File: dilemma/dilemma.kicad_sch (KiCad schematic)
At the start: 72 parts, among them J2 Serial, J4 Conn_01x01_Female, J5 S3B-PH-SM4-TB(LF)(SN), J7 trackball, SW1 SW_Push, SW10 SW_Push, SW11 SW_Push, SW12 SW_Push, SW13 SW_Push, SW14 SW_Push, SW15 SW_Push, SW16 SW_Push, SW17 SW_Push, SW2 SW_Push, SW26 SW_SPST, SW3 SW_Push, SW37 SW_SPST, SW4 SW_Push, SW5 SW_Push, SW6 SW_Push, SW7 SW_Push, SW8 SW_Push, SW9 SW_Push, U2 eliteC

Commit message: add battery connector
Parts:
- added H5, H6, H7, H8, H9: M4, footprints:MountingHole_3mm_Pad_thin, symbol Mechanical:MountingHole_Pad
- added J1: S3B-PH-SM4-TB(LF)(SN), Connector_JST:JST_PH_S3B-PH-SM4-TB_1x03-1MP_P2.00mm_Horizontal, symbol Connector:Conn_01x03_Female
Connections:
- net GND: now also H5.1, H6.1, H7.1, H8.1, H9.1
- net GND2: now also J1.1 (Pin_1), J1.3 (Pin_3)
- net bat_l: now also J1.2 (Pin_2)
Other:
- note added: "Mod screws"
- moved on the sheet: BT1, H1, H2, H3, H4, PSW1

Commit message: silkscreen
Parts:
- O2: footprint swoop:OLED_jumpers -> footprints:PinHeader_1x04_P2.54mm_Vertical
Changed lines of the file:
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@@
     (property "Reference" "O2" (id 0) (at 299.72 150.8275 0))
     (property "Value" "OLED" (id 1) (at 300.99 153.3675 0))
-    (property "Footprint" "swoop:OLED_jumpers" (id 2) (at 295.91 151.638 0)
+    (property "Footprint" "footprints:PinHeader_1x04_P2.54mm_Vertical" (id 2) (at 295.91 151.638 0)
       (effects (font (size 1.27 1.27)) hide)
     )
@@
     )
     (path "/c51d5d6e-3b88-4f8e-8052-c5e71c69581c"
-      (reference "O2") (unit 1) (value "OLED") (footprint "swoop:OLED_jumpers")
+      (reference "O2") (unit 1) (value "OLED") (footprint "footprints:PinHeader_1x04_P2.54mm_Vertical")
     )
     (path "/7b8c700f-e98a-4d4d-a6e4-baf976482a3f"

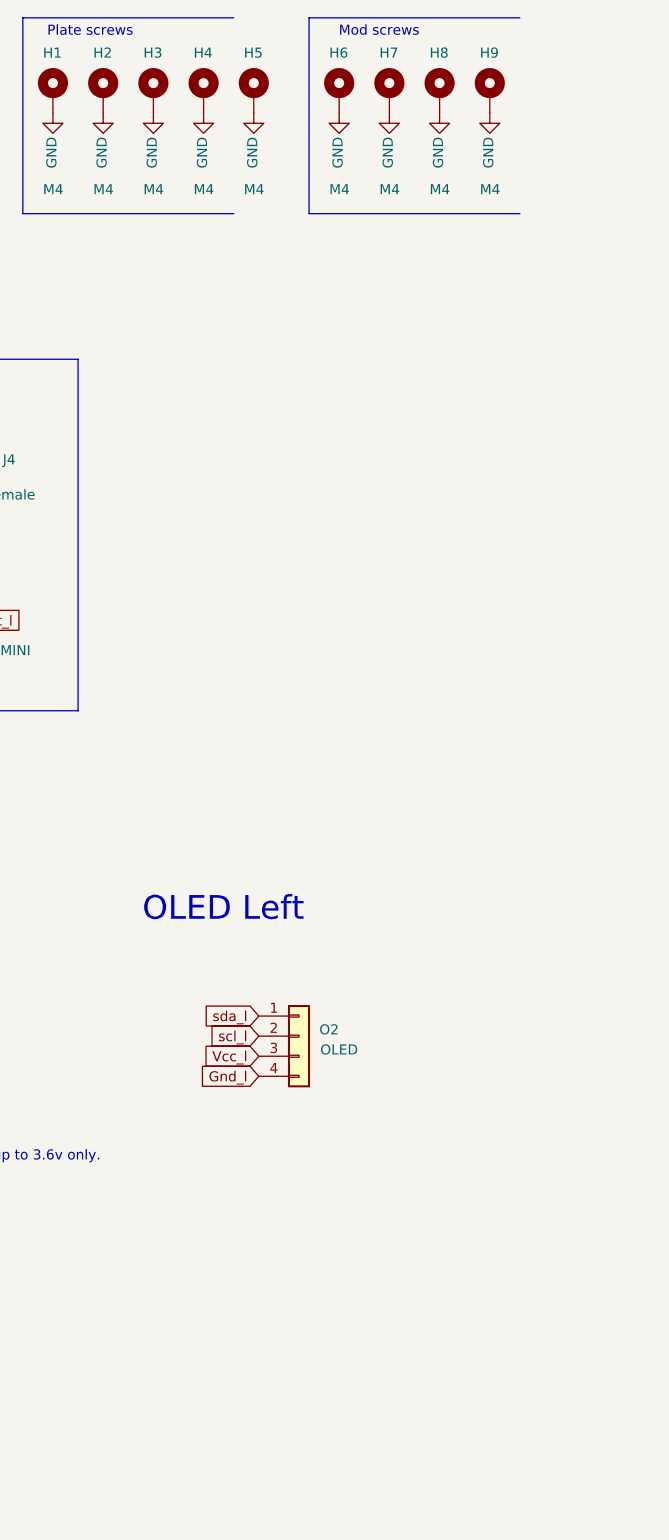
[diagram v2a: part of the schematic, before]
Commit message: trackpad connector reversible
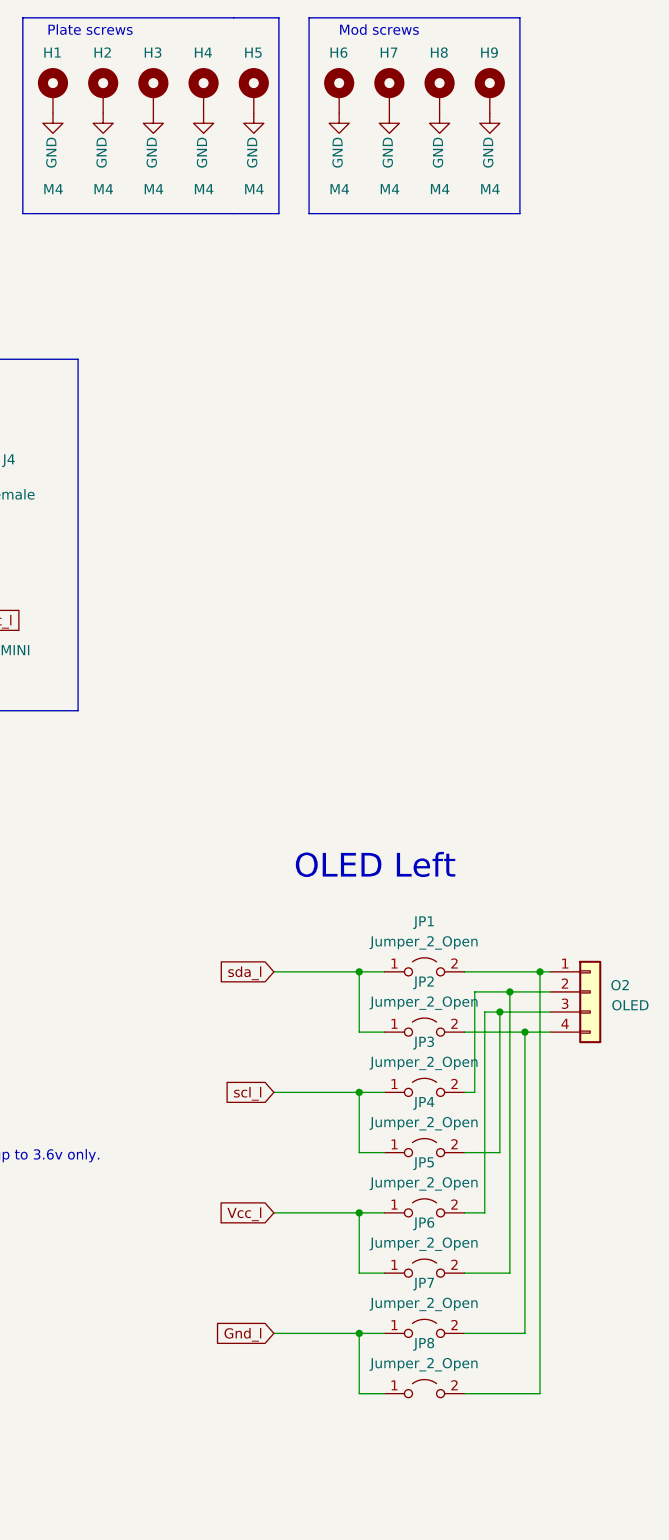
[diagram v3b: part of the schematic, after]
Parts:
- added JP1, JP2, JP3, JP4, JP5, JP6, JP7, JP8: Jumper_2_Open, footprints:SolderJumper-2_P1.3mm_Open_RoundedPad1.0x1.5mm, symbol Jumper:Jumper_2_Open
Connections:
- net +5VL: now also JP5.1 (A), JP6.1 (A); no longer O2.3 (Pin_3)
- net GND2: now also JP7.1 (A), JP8.1 (A); no longer O2.4 (Pin_4)
- net scl_l: now also JP3.1 (A), JP4.1 (A); no longer O2.2 (Pin_2)
- net sda_l: now also JP1.1 (A), JP2.1 (A); no longer O2.1 (Pin_1)
- new net: JP3.2 (B), JP6.2 (B), O2.2 (Pin_2)
- new net: JP4.2 (B), JP5.2 (B), O2.3 (Pin_3)
- new net: JP2.2 (B), JP7.2 (B), O2.4 (Pin_4)
- new net: JP1.2 (B), JP8.2 (B), O2.1 (Pin_1)
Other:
- moved on the sheet: O2

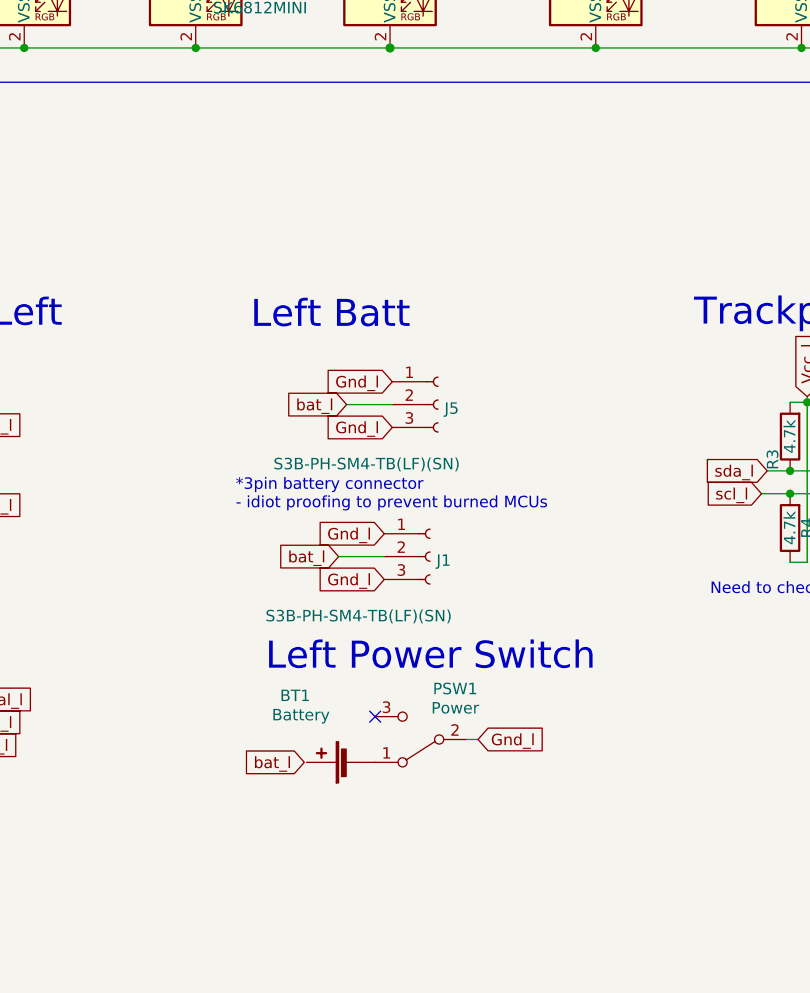
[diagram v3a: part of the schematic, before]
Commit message: Added battery THT and the most common power switch used for wireless builds
Added battery THT and the most common power switch used for wireless builds
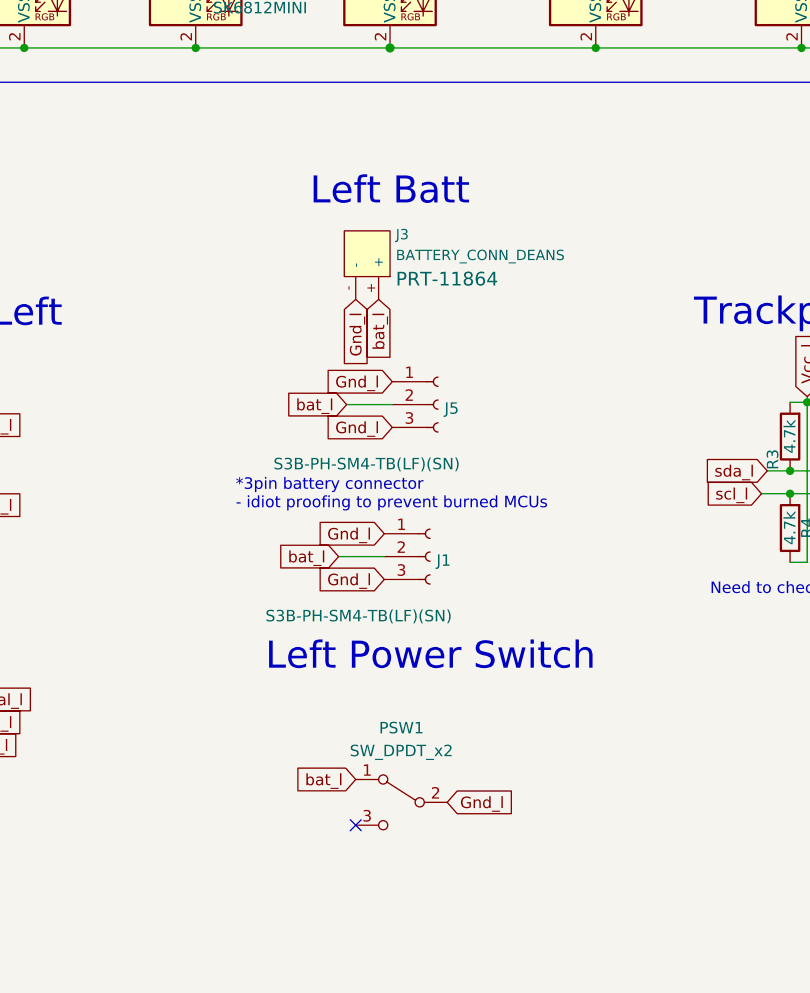
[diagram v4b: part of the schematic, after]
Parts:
- removed BT1: Battery, swoop:Battery_pads_reversible, symbol Device:Battery_Cell
- removed PSW1: Power, swoop:Power, symbol Switch:SW_SPDT
- added J3: BATTERY_CONN_DEANS, Connectors:1X02_LOCK, symbol SparkFun-Connectors:BATTERY_CONN_DEANS
- added PSW1: SW_DPDT_x2, used_footprints:Switch_MSK-12C01-07, symbol jiran-ble:SW_DPDT
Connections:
- net GND2: now also J3.-, PSW1.2 (B)
- net bat_l: now also J3.+, PSW1.1 (A)
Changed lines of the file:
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@@
   (junction (at 78.74 48.26) (diameter 0) (color 0 0 0 0)
   )
-  (no_connect (at 174.879 180.975))
+  (no_connect (at 172.72 193.04))
   (no_connect (at 128.27 176.53))
   (no_connect (at 43.18 181.61))
@@
     (stroke (width 0) (type solid) (color 0 0 0 0))
   )
-  (wire (pts (xy 185.039 183.515) (xy 186.309 183.515))
-    (stroke (width 0) (type default) (color 0 0 0 0))
-  )
   (wire (pts (xy 135.89 35.56) (xy 162.56 35.56))
     (stroke (width 0) (type default) (color 0 0 0 0))
@@
     (effects (font (size 3 3)) (justify left bottom))
   )
-  (text "Left Batt" (at 161.036 138.176 0)
+  (text "Left Batt" (at 167.64 124.46 0)
     (effects (font (size 3 3)) (justify left bottom))
   )
@@
     )
   )
-  (global_label "bat_l" (shape input) (at 167.005 186.055 180)
+  (global_label "bat_l" (shape input) (at 172.72 187.96 180)
     (effects (font (size 1.27 1.27)) (justify right))
-    (property "Intersheet References" "${INTERSHEET_REFS}" (id 0) (at 290.195 316.865 0)
+    (property "Intersheet References" "${INTERSHEET_REFS}" (id 0) (at 295.91 318.77 0)
       (effects (font (size 1.27 1.27)) hide)
     )
@@
     )
   )
+  (global_label "bat_l" (shape input) (at 175.26 134.62 270)
+    (effects (font (size 1.27 1.27)) (justify right))
+    (property "Intersheet References" "${INTERSHEET_REFS}" (id 0) (at 306.07 11.43 0)
+      (effects (font (size 1.27 1.27)) hide)
+    )
+  )
   (global_label "scl_l" (shape input) (at 217.805 156.21 180)
     (effects (font (size 1.27 1.27)) (justify right))
@@
     )
   )
+  (global_label "Gnd_l" (shape input) (at 172.72 134.62 270)
+    (effects (font (size 1.27 1.27)) (justify right))
+    (property "Intersheet References" "${INTERSHEET_REFS}" (id 0) (at 242.57 11.43 0)
+      (effects (font (size 1.27 1.27)) hide)
+    )
+  )
   (global_label "miso_l" (shape input) (at 68.58 168.91 0)
     (effects (font (size 1.27 1.27)) (justify left))
@@
     )
   )
-  (global_label "Gnd_l" (shape input) (at 186.309 183.515 0)
+  (global_label "Gnd_l" (shape input) (at 182.88 190.5 0)
     (effects (font (size 1.27 1.27)) (justify left))
-    (property "Intersheet References" "${INTERSHEET_REFS}" (id 0) (at 63.119 113.665 0)
+    (property "Intersheet References" "${INTERSHEET_REFS}" (id 0) (at 59.69 120.65 0)
       (effects (font (size 1.27 1.27)) hide)
     )
@@
     (pin "2")
   )
+  (symbol (lib_id "SparkFun-Connectors:BATTERY_CONN_DEANS") (at 172.72 132.08 270) (unit 1)
+    (in_bom yes) (on_board yes) (fields_autoplaced)
+    (property "Reference" "J3" (id 0) (at 177.165 127.4095 90)
+      (effects (font (size 1.143 1.143)) (justify left))
+    )
+    (property "Value" "BATTERY_CONN_DEANS" (id 1) (at 177.165 129.7181 90)
+      (effects (font (size 1.143 1.143)) (justify left))
+    )
+    (property "Footprint" "Connectors:1X02_LOCK" (id 2) (at 180.34 132.08 0)
+      (effects (font (size 0.508 0.508)) hide)
+    )
+    (property "Datasheet" "" (id 3) (at 172.72 132.08 0)
+      (effects (font (size 1.27 1.27)) hide)
+    )
+    (property "Field4" "PRT-11864" (id 4) (at 177.165 132.3691 90)
+      (effects (font (size 1.524 1.524)) (justify left))
+    )
+    (pin "+")
+    (pin "-")
+  )
   (symbol (lib_id "LED:SK6812MINI") (at 222.25 99.06 0) (unit 1)
     (in_bom yes) (on_board yes)
@@
     (pin "2")
   )
-  (symbol (lib_id "Switch:SW_SPDT") (at 179.959 183.515 180) (unit 1)
-    (in_bom yes) (on_board yes)
-    (property "Reference" "PSW1" (id 0) (at 183.769 177.8974 0))
-    (property "Value" "Power" (id 1) (at 183.769 180.0375 0))
-    (property "Footprint" "swoop:Power" (id 2) (at 179.959 183.515 0)
-      (effects (font (size 1.27 1.27)) hide)
-    )
-    (property "Datasheet" "~" (id 3) (at 179.959 183.515 0)
-      (effects (font (size 1.27 1.27)) hide)
-    )
-    (pin "1")
-    (pin "2")
-    (pin "3")
-  )
   (symbol (lib_id "Connector:Conn_01x06_Female") (at 100.965 202.565 0) (unit 1)
     (in_bom yes) (on_board yes)
@@
     (pin "2")
   )
+  (symbol (lib_id "jiran-ble:SW_DPDT") (at 176.53 190.5 0) (mirror y) (unit 1)
+    (in_bom yes) (on_board yes)
+    (property "Reference" "PSW1" (id 0) (at 177.8 182.245 0))
+    (property "Value" "SW_DPDT_x2" (id 1) (at 177.8 184.785 0))
+    (property "Footprint" "used_footprints:Switch_MSK-12C01-07" (id 2) (at 175.895 182.88 0)
+      (effects (font (size 1.27 1.27)) hide)
+    )
+    (property "Datasheet" "" (id 3) (at 175.895 182.88 0)
+      (effects (font (size 1.27 1.27)) hide)
+    )
+    (property "LCSC" "C431540" (id 4) (at 176.53 190.5 0)
+      (effects (font (size 1.27 1.27)) hide)
+    )
+    (pin "1")
+    (pin "2")
+    (pin "3")
+  )
   (symbol (lib_id "Device:D") (at 124.46 48.26 180) (unit 1)
     (in_bom yes) (on_board yes)
@@
     (pin "2")
   )
-  (symbol (lib_id "Device:Battery_Cell") (at 172.339 186.055 90) (unit 1)
-    (in_bom yes) (on_board yes)
-    (property "Reference" "BT1" (id 0) (at 165.989 178.6594 90))
-    (property "Value" "Battery" (id 1) (at 166.624 180.7995 90))
-    (property "Footprint" "swoop:Battery_pads_reversible" (id 2) (at 170.815 186.055 90)
-      (effects (font (size 1.27 1.27)) hide)
-    )
-    (property "Datasheet" "~" (id 3) (at 170.815 186.055 90)
-      (effects (font (size 1.27 1.27)) hide)
-    )
-    (pin "1")
-    (pin "2")
-  )
   (symbol (lib_id "Switch:SW_Push") (at 217.17 46.99 0) (unit 1)
     (in_bom yes) (on_board yes)
@@
       (reference "#PWR0107") (unit 1) (value "GND") (footprint "")
     )
-    (path "/9e8006cb-49f0-44ed-b39a-9f9d999f305f"
-      (reference "BT1") (unit 1) (value "Battery") (footprint "swoop:Battery_pads_reversible")
-    )
     (path "/1a1ab757-51de-4969-8924-8675206b3aa2"
       (reference "C1") (unit 1) (value "C") (footprint "")
@@
       (reference "J2") (unit 1) (value "Serial") (footprint "footprints:Jack_3.5mm_PJ320E_Horizontal_reversible")
     )
+    (path "/33a2f796-a38b-4191-afd9-29b38b8cb7e2"
+      (reference "J3") (unit 1) (value "BATTERY_CONN_DEANS") (footprint "Connectors:1X02_LOCK")
+    )
     (path "/8c327c2b-4d0a-43fd-a6c0-7a1543044924"
       (reference "J4") (unit 1) (value "Conn_01x01_Female") (footprint "")
@@
       (reference "O3") (unit 1) (value "trackpad") (footprint "footprints:PinHeader_1x04_P2.54mm_Vertical")
     )
-    (path "/490427c5-7c38-4754-bcb1-0cc9dfe9dad4"
-      (reference "PSW1") (unit 1) (value "Power") (footprint "swoop:Power")
+    (path "/59d2370e-e0ba-45a7-99f1-84fa16580e24"
+      (reference "PSW1") (unit 1) (value "SW_DPDT_x2") (footprint "used_footprints:Switch_MSK-12C01-07")
     )
     (path "/74b3aa64-9363-448b-93d6-0b22421aa5c3"

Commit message: cleanup
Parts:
- removed C1: C, symbol Device:C
- removed D1, D11, D12, D16, D17, D2, D21, D22, D23, D27, D28, D29, D31, D32, D34, D6, D7: SK6812MINI, symbol LED:SK6812MINI
- removed J4: Conn_01x01_Female, symbol Connector:Conn_01x01_Female
- removed O3: trackpad, footprints:PinHeader_1x04_P2.54mm_Vertical, symbol Connector_Generic:Conn_01x04
- removed R1: R, symbol Device:R
- removed R8: 5.1k, footprints:R_1206_handsolder, symbol Device:R
- R3, R4: footprint reversible-kicad-footprints:R-0805_2012Metric -> footprints:R_1206_handsolder_reversible
- R7: footprint footprints:R_1206_handsolder -> footprints:R_1206_handsolder_reversible
- U2: footprint footprints:Elite-C -> local-libraries:pro-micro
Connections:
- net GND2 is gone; now on net GND: J1.1 (Pin_1), J1.3 (Pin_3), J2.R1, J3.-, J5.1 (Pin_1), J5.3 (Pin_3), JP7.1 (A), JP8.1 (A), PSW1.2 (B), SW26.2 (B), SW37.2 (B), U2.23 (GND), U2.3 (GND), U2.4 (GND)
- net hand is gone; now on net GND: R7.1, U2.20 (F4)
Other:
- note added: "Pull ups for trackpad"
- note removed: "Left"
- note removed: "Need to check how to power Cirque since it's rated up to 3.6v only."
- note removed: "RGB - plate and thumb cluster"
- note removed: "Trackpad Left"
- moved on the sheet: J1, J2, J3, J5, J7, JP1, JP2, JP3, JP4, JP5, JP6, JP7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

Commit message: clean up battery tht connector
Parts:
- J3: footprint Connectors:1X02_LOCK -> local-libraries:battery_connector_THT
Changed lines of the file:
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@@
       (effects (font (size 1.143 1.143)) (justify left))
     )
-    (property "Footprint" "Connectors:1X02_LOCK" (id 2) (at 184.15 83.82 0)
+    (property "Footprint" "local-libraries:battery_connector_THT" (id 2) (at 184.15 83.82 0)
       (effects (font (size 0.508 0.508)) hide)
     )
@@
     )
     (path "/33a2f796-a38b-4191-afd9-29b38b8cb7e2"
-      (reference "J3") (unit 1) (value "BATTERY_CONN_DEANS") (footprint "Connectors:1X02_LOCK")
+      (reference "J3") (unit 1) (value "BATTERY_CONN_DEANS") (footprint "local-libraries:battery_connector_THT")
     )
     (path "/0024d4dc-bd5d-4def-a2be-39a78e329b8f"

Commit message: Schematic reference update
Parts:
- PSW1: footprint used_footprints:Switch_MSK-12C01-07 -> local-libraries:Switch_MSK-12C01-07
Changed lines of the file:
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@@
     (property "Reference" "PSW1" (id 0) (at 179.07 145.415 0))
     (property "Value" "SW_DPDT_x2" (id 1) (at 179.07 147.955 0))
-    (property "Footprint" "used_footprints:Switch_MSK-12C01-07" (id 2) (at 177.165 146.05 0)
+    (property "Footprint" "local-libraries:Switch_MSK-12C01-07" (id 2) (at 177.165 146.05 0)
       (effects (font (size 1.27 1.27)) hide)
     )
@@
     )
     (path "/59d2370e-e0ba-45a7-99f1-84fa16580e24"
-      (reference "PSW1") (unit 1) (value "SW_DPDT_x2") (footprint "used_footprints:Switch_MSK-12C01-07")
+      (reference "PSW1") (unit 1) (value "SW_DPDT_x2") (footprint "local-libraries:Switch_MSK-12C01-07")
     )
     (path "/4acaff23-3513-4df1-ad8e-582535069bb0"

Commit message: chopped up
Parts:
- J1, J5: footprint Connector_JST:JST_PH_S3B-PH-SM4-TB_1x03-1MP_P2.00mm_Horizontal -> Connector_JST:JST_SH_BM03B-SRSS-TB_1x03-1MP_P1.00mm_Vertical
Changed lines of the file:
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@@
       (effects (font (size 1.27 1.27)) (justify left))
     )
-    (property "Footprint" "Connector_JST:JST_PH_S3B-PH-SM4-TB_1x03-1MP_P2.00mm_Horizontal" (id 2) (at 186.944 99.314 0)
+    (property "Footprint" "Connector_JST:JST_SH_BM03B-SRSS-TB_1x03-1MP_P1.00mm_Vertical" (id 2) (at 186.944 99.314 0)
       (effects (font (size 1.27 1.27)) hide)
     )
@@
       (effects (font (size 1.27 1.27)) (justify left))
     )
-    (property "Footprint" "Connector_JST:JST_PH_S3B-PH-SM4-TB_1x03-1MP_P2.00mm_Horizontal" (id 2) (at 186.055 116.205 0)
+    (property "Footprint" "Connector_JST:JST_SH_BM03B-SRSS-TB_1x03-1MP_P1.00mm_Vertical" (id 2) (at 186.055 116.205 0)
       (effects (font (size 1.27 1.27)) hide)
     )
@@
     )
     (path "/66955d3c-d746-41bf-9f85-512a3bc00115"
-      (reference "J1") (unit 1) (value "S3B-PH-SM4-TB(LF)(SN)") (footprint "Connector_JST:JST_PH_S3B-PH-SM4-TB_1x03-1MP_P2.00mm_Horizontal")
+      (reference "J1") (unit 1) (value "S3B-PH-SM4-TB(LF)(SN)") (footprint "Connector_JST:JST_SH_BM03B-SRSS-TB_1x03-1MP_P1.00mm_Vertical")
     )
     (path "/d91dbeff-81c6-4fb8-bb3a-36a08837981c"
@@
     )
     (path "/0024d4dc-bd5d-4def-a2be-39a78e329b8f"
-      (reference "J5") (unit 1) (value "S3B-PH-SM4-TB(LF)(SN)") (footprint "Connector_JST:JST_PH_S3B-PH-SM4-TB_1x03-1MP_P2.00mm_Horizontal")
+      (reference "J5") (unit 1) (value "S3B-PH-SM4-TB(LF)(SN)") (footprint "Connector_JST:JST_SH_BM03B-SRSS-TB_1x03-1MP_P1.00mm_Vertical")
     )
     (path "/49e8e7c0-6978-4c62-8c73-5e4e14bca074"
